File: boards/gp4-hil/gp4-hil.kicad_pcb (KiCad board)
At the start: 4 copper layers, 160 x 62 mm, 452 parts, among them J1 BEL_FUSE_0826-1G1T-23-F, J2 XILINX_JTAG, J3 XILINX_JTAG_ICESIDE, J4 XILINX_JTAG_ICESIDE, K1 CONN_3_PWROUT, P1 GPAK_ZIF, P2 2x10 HEADER, Q1 SSM6N58NU, Q11 SSM6N58NU, Q12 DMP2069UFY4, Q13 SSM6N58NU, Q14 SSM6N58NU, Q15 SSM6N58NU, Q16 SSM6N58NU, Q17 SSM6N58NU, Q18 SSM6N58NU, Q19 SSM6N58NU, Q20 SSM6N58NU, Q21 SSM6N58NU, Q22 DMP2069UFY4, U1 MIC2288-DFN, U10 AD9609, U11 DAC084S085, U12 DAC084S085, U13 DAC084S085, U14 DAC084S085, U15 TS3A4751, U16 TS3A4751, U17 TS3A4751, U18 TS3A4751, U19 TS3A4751, U2 XC7A100T-1FTG256C, U20 SIP32408, U21 SIP32408, U22 SIP32408, U23 SIP32408, U24 SIP32408, U25 TS3A4751, U26 TS3A4751, U27 TS3A4751, U28 TS3A4751, U29 TXB0104RUT, U3 LTC3374-QFN, U30 TXB0104RUT, U31 ADA4937-2, U32 SIP32408, U33 125 MHz, U34 INA199A2RSW, U35 INA199A2RSW, U36 INA199A2RSW, U4 SIP32408, U5 KSZ9031RN, U6 W25Q32FW, U7 25 MHz, U8 ADG726, U9 AD9609

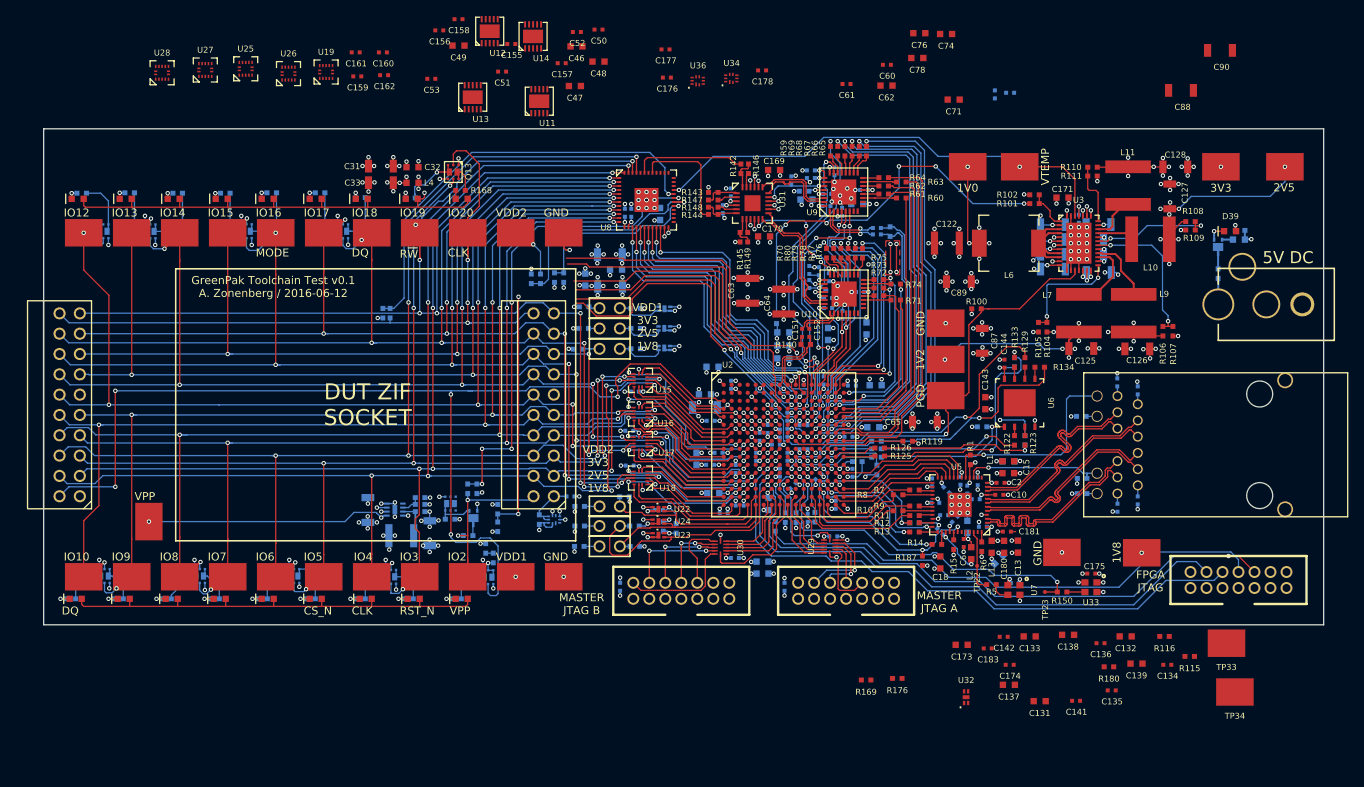
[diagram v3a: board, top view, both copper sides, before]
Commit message: Continued routing, began DAC stuff
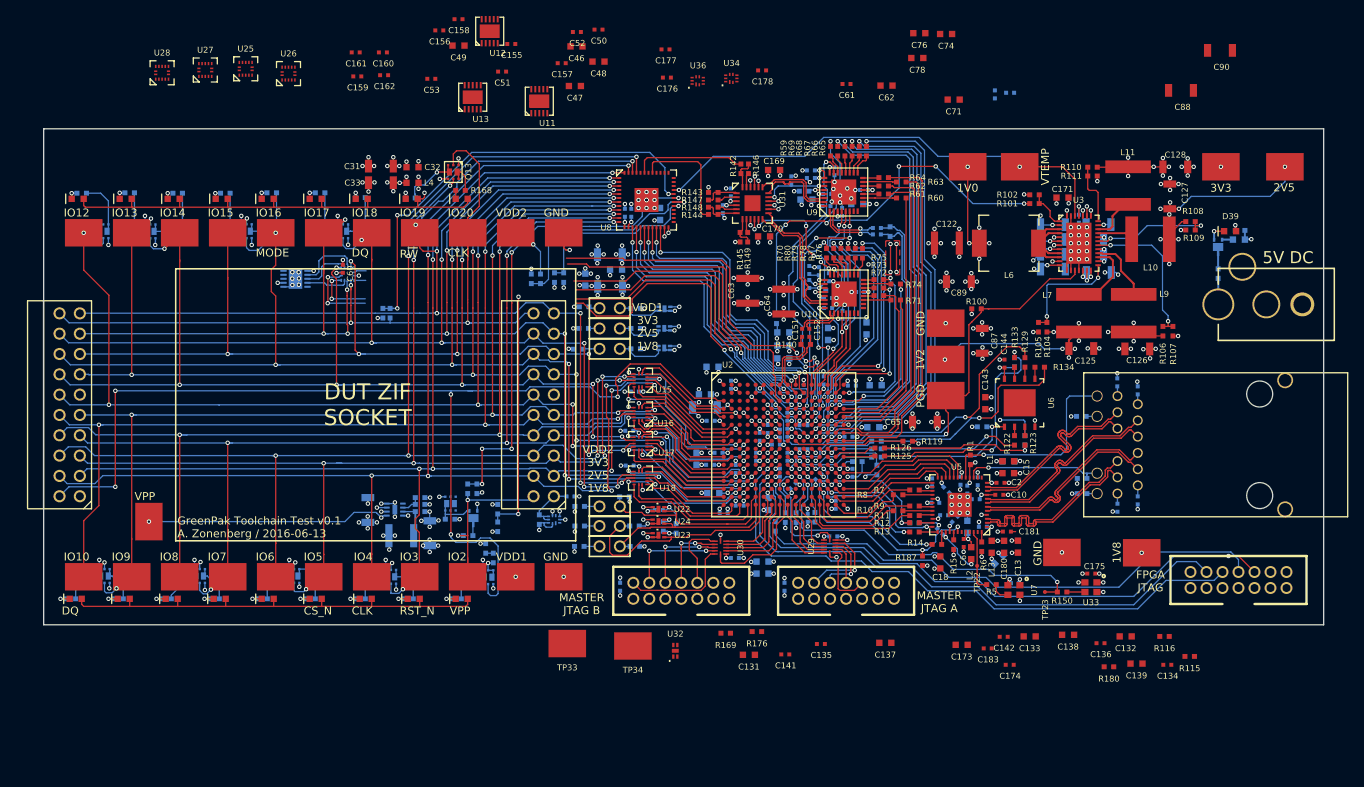
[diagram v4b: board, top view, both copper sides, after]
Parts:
- U14, U19: moved to B.Cu
- moved TP33 82.4 mm to (86.5, 122.3)
- moved TP34 75.5 mm to (94.7, 122.7)
- moved C60 72.6 mm to (58.4, 75.5), turned to 270 degrees
- moved U14 42.4 mm to (52.5, 76.8), turned to 270 degrees
- moved C141 36.8 mm to (113.7, 123.7)
- moved U32 36.8 mm to (100.0, 123.2)
- moved C131 36.8 mm to (109.2, 123.8)
- moved C135 36.8 mm to (118.2, 122.4)
- moved U19 25.4 mm to (59.0, 76.2), turned to 180 degrees
- moved R169 18.5 mm to (106.2, 121.0)
- moved R176 18.5 mm to (110.2, 120.8)
- moved C137 16.3 mm to (126.2, 122.2)
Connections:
- U13 pad 4: /Analog IO/GPIO14_ASIG -> (no net)
- U13 pad 5: /Analog IO/GPIO15_ASIG -> (no net)
- U14 pad 2: /Analog IO/GPIO17_ASIG -> /Analog IO/GPIO15_ASIG
- U14 pad 3: (no net) -> /Analog IO/GPIO14_ASIG
- U14 pad 4: (no net) -> /Analog IO/GPIO17_ASIG
- U19 pad 10: /Analog IO/GPIO6_ASIG -> /Analog IO/GPIO15_ASIG
- U19 pad 11: /Analog IO/DUT_GPIO6 -> /Analog IO/DUT_GPIO15
- U19 pad 12: /Analog IO/GPIO6_AEN -> /Analog IO/GPIO15_AEN
- U19 pad 3: /Analog IO/DUT_GPIO4 -> /Analog IO/DUT_GPIO17
- U19 pad 4: /Analog IO/GPIO4_ASIG -> /Analog IO/GPIO17_ASIG
- U19 pad 5: /Analog IO/GPIO4_AEN -> /Analog IO/GPIO17_AEN
- U19 pad 6: /Analog IO/GPIO5_AEN -> /Analog IO/GPIO14_AEN
- U19 pad 8: /Analog IO/DUT_GPIO5 -> /Analog IO/DUT_GPIO14
- U19 pad 9: /Analog IO/GPIO5_ASIG -> /Analog IO/GPIO14_ASIG
- U2 pad A2: (no net) -> /Analog IO/GPIO17_AEN
- U2 pad A3: (no net) -> /Analog IO/GPIO6_AEN
- U2 pad A4: (no net) -> /Analog IO/GPIO9_AEN
- U2 pad A5: /Analog IO/GPIO17_AEN -> /Analog IO/GPIO4_AEN
- U2 pad B1: (no net) -> /Analog IO/GPIO10_AEN
- U2 pad B2: (no net) -> /Analog IO/GPIO15_AEN
- U2 pad B4: (no net) -> /Analog IO/GPIO3_AEN
- U2 pad B5: /Analog IO/GPIO9_AEN -> /Analog IO/GPIO12_AEN
- U2 pad B6: /Analog IO/GPIO6_AEN -> (no net)
- U2 pad B7: /Analog IO/GPIO10_AEN -> (no net)
- U2 pad C2: (no net) -> /Analog IO/GPIO8_AEN
- U2 pad C3: (no net) -> /Analog IO/GPIO14_AEN
- U2 pad C4: (no net) -> /Analog IO/GPIO7_AEN
- U2 pad E5: /Analog IO/GPIO15_AEN -> (no net)
- U2 pad F3: /Analog IO/GPIO4_AEN -> (no net)
- U2 pad F4: /Analog IO/GPIO3_AEN -> (no net)
- U2 pad G4: /Analog IO/GPIO8_AEN -> (no net)
- U2 pad G5: /Analog IO/GPIO7_AEN -> (no net)
- U2 pad H5: /Analog IO/GPIO12_AEN -> (no net)
- U2 pad J5: /Analog IO/GPIO14_AEN -> (no net)
- U26 pad 10: /Analog IO/GPIO15_ASIG -> /Analog IO/GPIO4_ASIG
- U26 pad 11: /Analog IO/DUT_GPIO15 -> /Analog IO/DUT_GPIO4
- U26 pad 12: /Analog IO/GPIO15_AEN -> /Analog IO/GPIO4_AEN
- U26 pad 6: /Analog IO/GPIO14_AEN -> /Analog IO/GPIO5_AEN
- U26 pad 8: /Analog IO/DUT_GPIO14 -> /Analog IO/DUT_GPIO5
- U26 pad 9: /Analog IO/GPIO14_ASIG -> /Analog IO/GPIO5_ASIG
- U28 pad 1: /Analog IO/DUT_GPIO17 -> /Analog IO/DUT_GPIO6
- U28 pad 13: /Analog IO/GPIO17_AEN -> /Analog IO/GPIO6_AEN
- U28 pad 2: /Analog IO/GPIO17_ASIG -> /Analog IO/GPIO6_ASIG
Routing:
- net /Analog IO/A3V3: track 61.3 -> 108.8 mm, vias 16 -> 18
- net /Analog IO/DUT_VDD1: track 189.5 -> 220.8 mm, vias 20 -> 22
- net /Analog IO/GND: track 1412.2 -> 1429.2 mm, vias 287 -> 294
- net /Analog IO/DUT_GPIO14: track 145.2 -> 162.0 mm, vias 8 -> 10
- net /Analog IO/DUT_GPIO15: track 140.7 -> 154.8 mm, vias 8 -> 10
- net /Analog IO/DUT_GPIO19: track 150.9 -> 141.4 mm, vias 9 -> 8
- net /Analog IO/GPIO14_AEN: track 0.71 -> 9.72 mm, vias 1 -> 2
- net /Analog IO/GPIO17_AEN: track 0.00 -> 8.10 mm, vias 0 -> 2
- net /Analog IO/GPIO15_ASIG: track 0.00 -> 8.06 mm
- net /Analog IO/DUT_GPIO17: track 147.6 -> 154.4 mm, vias 8 -> 10
- net /Analog IO/GPIO14_ASIG: track 0.00 -> 6.48 mm
- net /Analog IO/DUT_GPIO20: track 91.0 -> 96.4 mm
- net /Analog IO/GPIO17_ASIG: track 0.00 -> 5.26 mm
- net /Digital IO/GPIO20_DEN: track 0.00 -> 1.58 mm
- net /Analog IO/ADC_GPIO20: track 54.0 -> 55.5 mm, vias 1 -> 3
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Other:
- board text added: "GreenPak Toolchain Test v0.1 A. Zonenberg / 2016-06-13"
- board text removed: "GreenPak Toolchain Test v0.1 A. Zonenberg / 2016-06-12"

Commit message: More DAC work. 184 unrouted.
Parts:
- removed C162: 0.47 uF, azonenberg_pcb:EIA_0402_CAP_NOSILK
- removed U28: TS3A4751, azonenberg_pcb:QFN_14_0.4MM_2x2MM_TI_RUC
- C159, C160, U11, U12, U13, U25, U26, U27: moved to B.Cu
- moved TP34 77.5 mm to (32.0, 77.0)
- moved U12 71.4 mm to (35.5, 104.1), turned to 270 degrees
- moved U11 58.6 mm to (51.5, 104.1), turned to 270 degrees
- moved C160 58.1 mm to (46.4, 104.0), turned to 90 degrees
- moved TP33 57.4 mm to (86.0, 65.0)
- moved U25 54.5 mm to (56.5, 104.0)
- moved C52 54.3 mm to (43.8, 77.8)
- moved U26 53.9 mm to (41.1, 104.0), turned to 90 degrees
- moved C159 50.7 mm to (57.2, 102.0)
- moved C157 47.3 mm to (46.4, 75.9), turned to 180 degrees
- moved U13 37.3 mm to (45.0, 76.7), turned to 90 degrees
- moved C158 36.7 mm to (53.8, 75.7), turned to 180 degrees
- moved C161 34.1 mm to (39.5, 75.8), turned to 180 degrees
- moved C53 31.8 mm to (51.0, 77.7)
- moved C50 26.6 mm to (65.6, 55.5)
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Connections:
- U2 pad C8: /Analog IO/DAC_B_DIN -> /Analog IO/DAC_C_DIN
- U2 pad D9: /Analog IO/DAC_C_DIN -> /Analog IO/DAC_B_DIN
- U25 pad 10: /Analog IO/GPIO10_ASIG -> /Analog IO/GPIO6_ASIG
- U25 pad 11: /Analog IO/DUT_GPIO10 -> /Analog IO/DUT_GPIO6
- U25 pad 12: /Analog IO/GPIO10_AEN -> /Analog IO/GPIO6_AEN
- U25 pad 3: /Analog IO/DUT_GPIO8 -> /Analog IO/DUT_GPIO4
- U25 pad 4: /Analog IO/GPIO8_ASIG -> /Analog IO/GPIO4_ASIG
- U25 pad 5: /Analog IO/GPIO8_AEN -> /Analog IO/GPIO4_AEN
- U25 pad 6: /Analog IO/GPIO9_AEN -> /Analog IO/GPIO5_AEN
- U25 pad 8: /Analog IO/DUT_GPIO9 -> /Analog IO/DUT_GPIO5
- U25 pad 9: /Analog IO/GPIO9_ASIG -> /Analog IO/GPIO5_ASIG
- U26 pad 10: /Analog IO/GPIO4_ASIG -> /Analog IO/GPIO10_ASIG
- U26 pad 11: /Analog IO/DUT_GPIO4 -> /Analog IO/DUT_GPIO10
- U26 pad 12: /Analog IO/GPIO4_AEN -> /Analog IO/GPIO10_AEN
- U26 pad 3: /Analog IO/DUT_GPIO13 -> /Analog IO/DUT_GPIO8
- U26 pad 4: /Analog IO/GPIO13_ASIG -> /Analog IO/GPIO8_ASIG
- U26 pad 5: /Analog IO/GPIO13_AEN -> /Analog IO/GPIO8_AEN
- U26 pad 6: /Analog IO/GPIO5_AEN -> /Analog IO/GPIO9_AEN
- U26 pad 8: /Analog IO/DUT_GPIO5 -> /Analog IO/DUT_GPIO9
- U26 pad 9: /Analog IO/GPIO5_ASIG -> /Analog IO/GPIO9_ASIG
- U27 pad 1: /Analog IO/DUT_GPIO12 -> /Analog IO/DUT_GPIO13
- U27 pad 13: /Analog IO/GPIO12_AEN -> /Analog IO/GPIO13_AEN
- U27 pad 2: /Analog IO/GPIO12_ASIG -> /Analog IO/GPIO13_ASIG
- U27 pad 3: (no net) -> /Analog IO/DUT_GPIO12
- U27 pad 4: (no net) -> /Analog IO/GPIO12_ASIG
- U27 pad 5: (no net) -> /Analog IO/GPIO12_AEN
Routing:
- net /Analog IO/DAC_SCLK: track 37.5 -> 87.7 mm, vias 2 -> 6
- net /Analog IO/DAC_SYNC_N: track 46.8 -> 96.3 mm, vias 2 -> 6
- net /Analog IO/DAC_D_DIN: track 49.9 -> 91.7 mm, vias 4 -> 5
- net /Analog IO/DAC_C_DIN: track 40.2 -> 77.9 mm
- net /Analog IO/GND: track 1429.2 -> 1454.3 mm, vias 294 -> 302
- net /Analog IO/GPIO17_AEN: track 8.10 -> 27.2 mm
- net /Analog IO/GPIO14_AEN: track 9.72 -> 28.8 mm
- net /Analog IO/DUT_GPIO13: track 143.3 -> 162.4 mm, vias 8 -> 11
- net /Digital IO/GPIO20_DIO: track 2.16 -> 21.1 mm
- net /Digital IO/GPIO20_DEN: track 1.58 -> 20.2 mm
- net /Analog IO/A3V3: track 108.8 -> 126.7 mm, vias 18 -> 21
- net /Analog IO/DUT_GPIO12: track 149.6 -> 166.6 mm, vias 8 -> 11
- net /Analog IO/GPIO13_ASIG: track 0.00 -> 2.52 mm
- net /Analog IO/GPIO12_ASIG: track 0.00 -> 2.41 mm
- net /Analog IO/DUT_GPIO5: track 164.0 -> 163.2 mm
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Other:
- board text added: "VDD2_EN"
- board text removed: "DAC isolation switching"

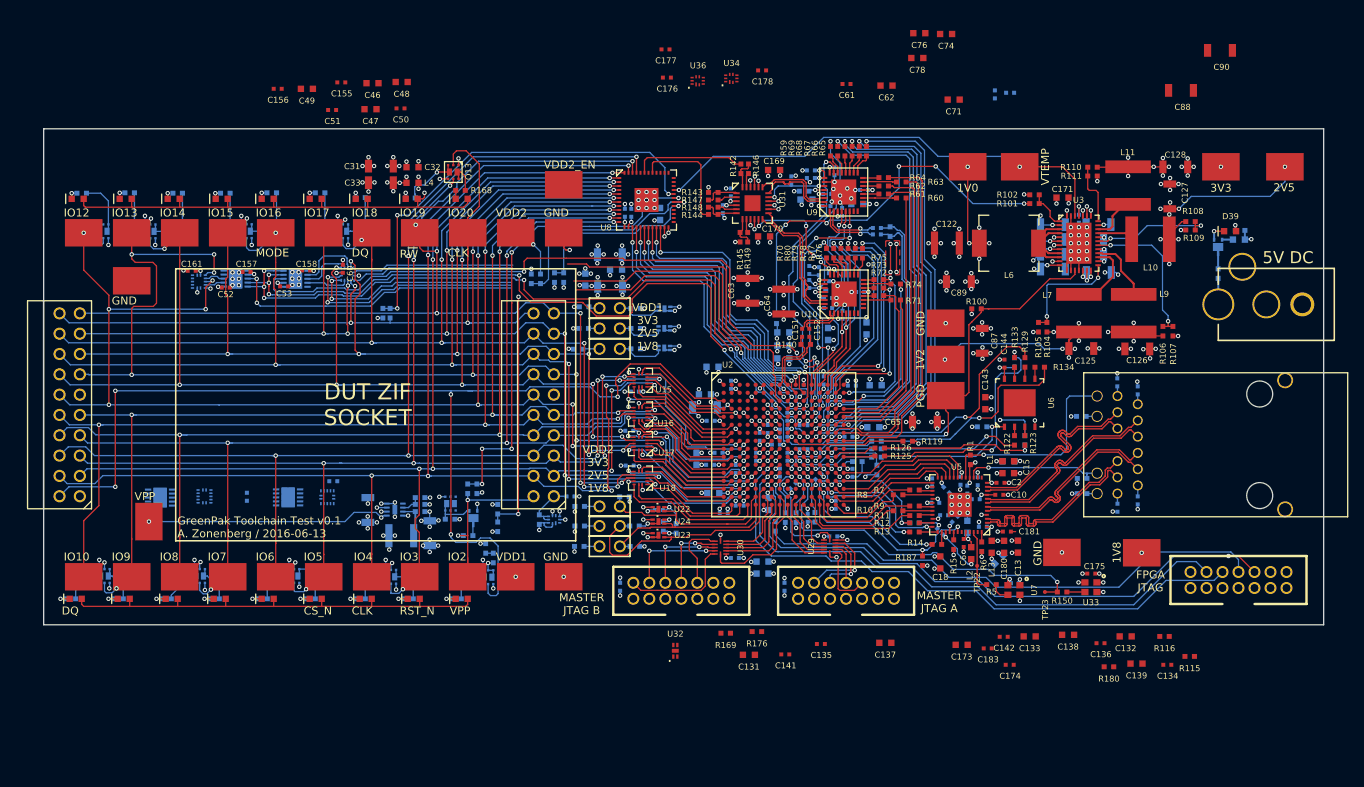
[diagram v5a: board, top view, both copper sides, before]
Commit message: Continued DAC routing. 150 unrouted nets.
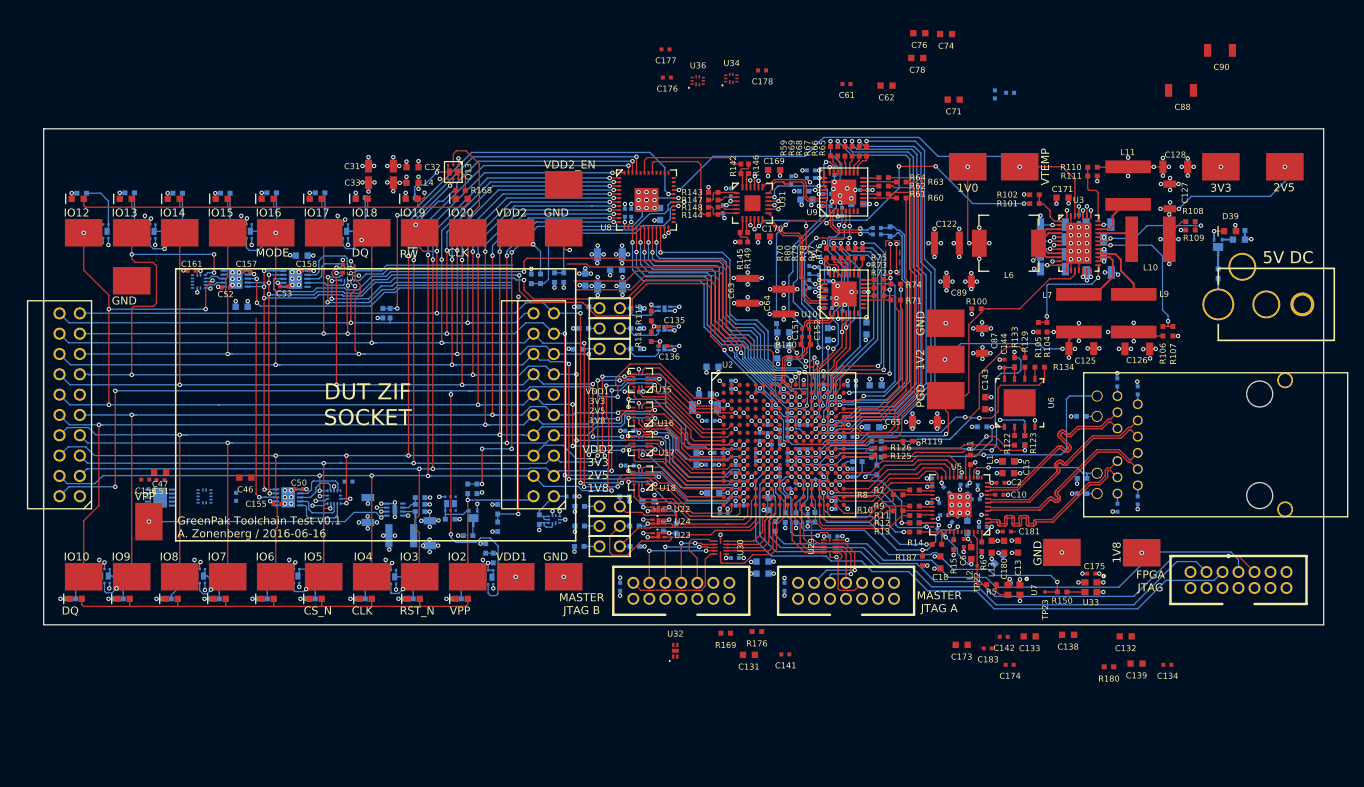
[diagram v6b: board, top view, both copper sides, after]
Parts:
- C137, C48, C49: moved to B.Cu
- moved R115 79.6 mm to (97.0, 81.4), turned to 270 degrees
- moved R116 74.3 mm to (97.0, 84.0), turned to 270 degrees
- moved C136 66.1 mm to (98.4, 85.2)
- moved C155 53.3 mm to (50.2, 104.9)
- moved C47 52.4 mm to (35.5, 100.9)
- moved C46 51.8 mm to (46.2, 101.6)
- moved C156 51.6 mm to (33.7, 101.8)
- moved C51 51.0 mm to (35.6, 101.9)
- moved C50 49.3 mm to (52.9, 103.0), turned to 180 degrees
- moved C135 44.3 mm to (98.3, 82.8)
- moved C48 34.5 mm to (45.8, 80.2), turned to 180 degrees
- moved C137 34.5 mm to (96.6, 104.5)
- moved C49 20.9 mm to (53.2, 73.8)
- moved C159 1.90 mm to (59.1, 102.1)
- moved C160 1.35 mm to (45.0, 104.0)
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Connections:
- U25 pad 1: /Analog IO/DUT_GPIO3 -> /Analog IO/DUT_GPIO4
- U25 pad 10: /Analog IO/GPIO6_ASIG -> /Analog IO/GPIO5_ASIG
- U25 pad 11: /Analog IO/DUT_GPIO6 -> /Analog IO/DUT_GPIO5
- U25 pad 12: /Analog IO/GPIO6_AEN -> /Analog IO/GPIO5_AEN
- U25 pad 13: /Analog IO/GPIO3_AEN -> /Analog IO/GPIO4_AEN
- U25 pad 2: /Analog IO/GPIO3_ASIG -> /Analog IO/GPIO4_ASIG
- U25 pad 3: /Analog IO/DUT_GPIO4 -> /Analog IO/DUT_GPIO3
- U25 pad 4: /Analog IO/GPIO4_ASIG -> /Analog IO/GPIO3_ASIG
- U25 pad 5: /Analog IO/GPIO4_AEN -> /Analog IO/GPIO3_AEN
- U25 pad 6: /Analog IO/GPIO5_AEN -> /Analog IO/GPIO6_AEN
- U25 pad 8: /Analog IO/DUT_GPIO5 -> /Analog IO/DUT_GPIO6
- U25 pad 9: /Analog IO/GPIO5_ASIG -> /Analog IO/GPIO6_ASIG
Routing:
- net /Analog IO/GND: track 1454.3 -> 1481.6 mm, vias 302 -> 312
- net /Analog IO/DAC_SYNC_N: track 96.3 -> 122.0 mm, vias 6 -> 7
- net /Analog IO/DAC_SCLK: track 87.7 -> 113.2 mm, vias 6 -> 7
- net /Analog IO/DAC_A_DIN: track 42.7 -> 67.4 mm, vias 2 -> 3
- net /Analog IO/A3V3: track 126.7 -> 146.9 mm, vias 21 -> 26
- net /Analog IO/DUT_VDD1: track 220.8 -> 237.8 mm, vias 22 -> 23
- net /Analog IO/GPIO6_ASIG: track 0.00 -> 7.57 mm
- net /Analog IO/GPIO3_ASIG: track 0.00 -> 6.95 mm
- net /Analog IO/DUT_GPIO6: track 166.9 -> 173.8 mm, vias 8 -> 10
- net /Analog IO/GPIO5_ASIG: track 0.00 -> 6.40 mm
- net /Analog IO/GPIO4_ASIG: track 0.00 -> 5.65 mm
- net /Analog IO/DUT_GPIO4: track 170.4 -> 173.3 mm, vias 8 -> 10
- net Net-(C135-Pad1): track 0.00 -> 2.82 mm, vias 0 -> 1
- net Net-(C136-Pad1): track 0.00 -> 2.40 mm, vias 0 -> 1
- net /Analog IO/GPIO5_AEN: track 0.00 -> 2.00 mm, vias 0 -> 1
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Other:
- board text added: "GreenPak Toolchain Test v0.1 A. Zonenberg / 2016-06-16"
- board text removed: "DACs"
- board text removed: "GreenPak Toolchain Test v0.1 A. Zonenberg / 2016-06-13"
